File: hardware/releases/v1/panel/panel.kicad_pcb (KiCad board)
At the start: 4 copper layers, 119 x 56 mm, 132 parts, among them J1 12-32V + RS485, J101 Main board, J102 XD_North, J103 XD_East, J104 XD_South, J105 XD_West, J106 PIEZO_NE, J107 PIEZO_NW, J108 PIEZO_SW, J109 PIEZO_SE, J110 DOME_SOCKET, J2 Crown board, J201 Probe T-Header SMD, J3 Probe board, J301 CROWN_RISER, J4 SEN55 PM, J401 Main board, J402 Reflector T-Socket SMD, Q1 AO3400A, Q401 AO3400A, SW1 SERVICE, U1 SCT2400TVBR, U101 SN74LVC2G04DBVR, U102 CD4052BM96, U103 TLV9062IDR, U104 LM393DR2G, U105 TLV9062IDR, U106 MMC5603NJ, U2 LM66100, U3 XIAO ESP32C6, U301 LTR-390UV-01, U302 VEML7700-TT, U4 BMP581, U401 SCD41-D-R2, U402 SGP41-D-R4, U403 SHT40-AD1F-R2, U404 LM393DR2G, U5 LSM6DS3TR-C, U6 AS3935-BQFT, U7 SP3485EN-L/TR, U8 SN74LVC2G04DBVR

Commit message: Add silkscreen connector labels to all PCB variants for improved assembly identification
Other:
- board text added: "+V GND A+ B-"
- board text added: "CROWN"
- board text added: "DOME"
- board text added: "MAIN"
- board text added: "PM"
- board text added: "PROBE"
- board text added: "REFLECTOR"
- board text added: "RST"

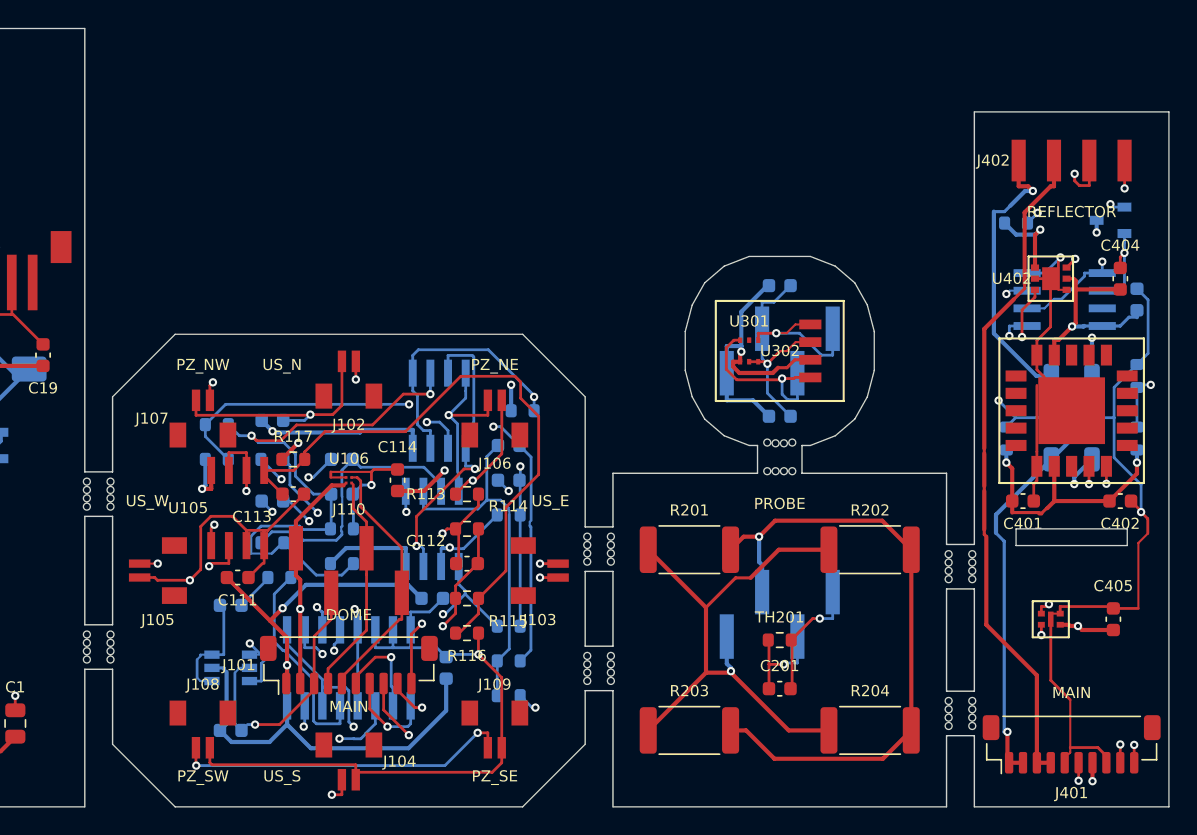
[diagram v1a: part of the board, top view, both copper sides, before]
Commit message: Upgrade dome PCB with enhanced light sensing capabilities: add TSL25911FN visible/NIR sensor and optional GUVB-C31SM UV-B sensor
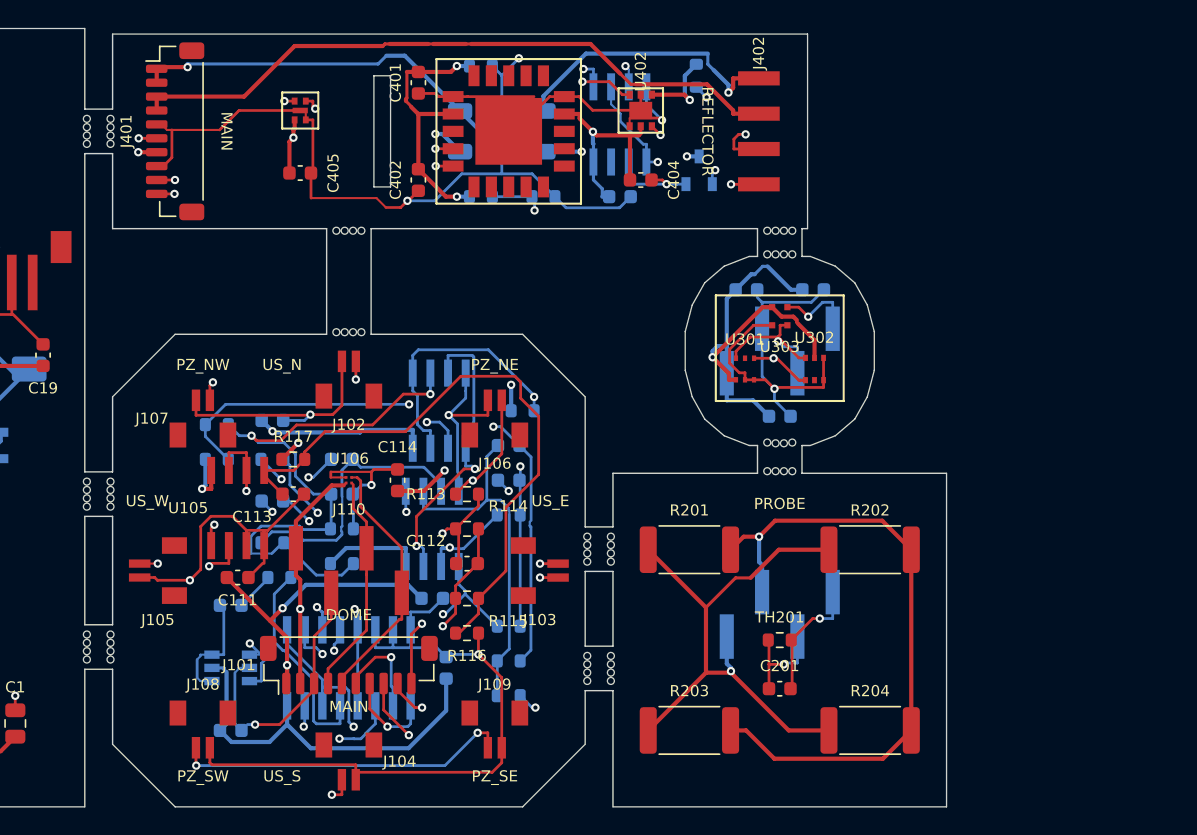
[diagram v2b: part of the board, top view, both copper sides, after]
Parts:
- added C303: 100n 50V, Capacitor_SMD:C_0603_1608Metric, B.Cu at (91.0, -28.1)
- added U303: GUVB-C31SM, gateway_fp:GenUV_GUVB-C31SM, F.Cu at (91.0, -35.3)
- U302: value VEML7700-TT -> TSL25911FN; footprint gateway_fp:Vishay_VEML7700-TT -> gateway_fp:AMS_TSL25911FN
- moved J401 78.1 mm to (47.5, -48.6), turned to -90 degrees
- moved C405 66.7 mm to (56.5, -45.6), turned to 0 degrees
- moved U403 65.2 mm to (56.5, -50.1), turned to -90 degrees
- moved C402 55.5 mm to (65.0, -45.1), turned to -90 degrees
- moved C401 52.9 mm to (65.0, -52.1), turned to -90 degrees
- moved R404 50.3 mm to (69.5, -43.9), turned to 0 degrees
- moved R401 49.9 mm to (68.0, -48.6), turned to -90 degrees
- moved R403 46.3 mm to (69.5, -53.3), turned to 0 degrees
- moved TH401 45.9 mm to (71.0, -48.6), turned to -90 degrees
- moved U401 45.2 mm to (71.5, -48.6), turned to -90 degrees
- moved R405 44.6 mm to (74.0, -43.9), turned to 0 degrees
- moved R402 41.9 mm to (74.0, -48.6), turned to -90 degrees
- moved C403 37.9 mm to (79.5, -43.9), turned to 0 degrees
- moved C404 35.2 mm to (81.0, -45.1), turned to 0 degrees
- moved U404 34.4 mm to (79.5, -49.1), turned to 0 degrees
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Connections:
- U302 pad 1: DOME_I2C_SDA -> DOME_I2C_SCL
- U302 pad 2: DOME_+3V3 -> (no net)
- U302 pad 4: DOME_I2C_SCL -> DOME_GND
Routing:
- net DOME_GND: track 16.5 -> 29.0 mm
- net DOME_+3V3: track 21.9 -> 33.3 mm
- net DOME_I2C_SCL: track 11.1 -> 14.2 mm, vias 1 -> 2
- net DOME_I2C_SDA: track 13.5 -> 11.7 mm
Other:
- board size 119 x 56 mm -> 103 x 56 mm

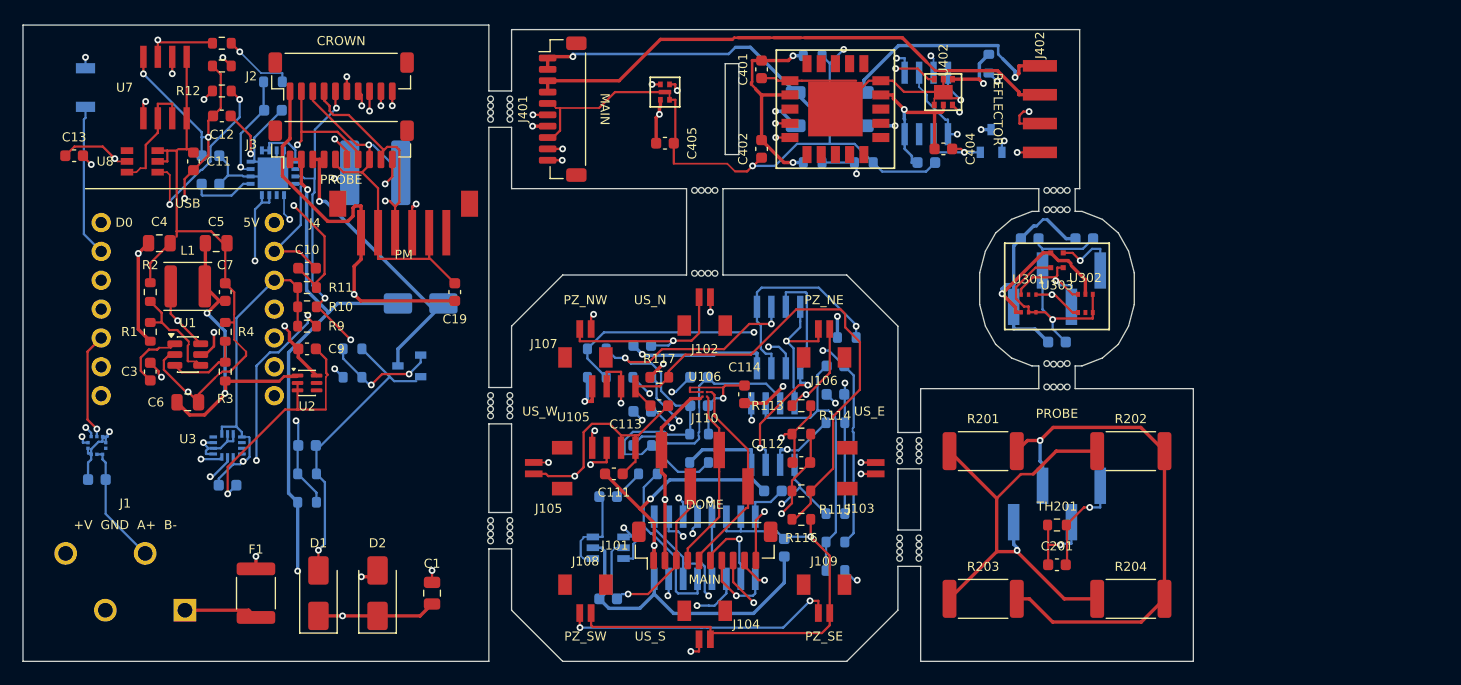
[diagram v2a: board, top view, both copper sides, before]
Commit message: Update enclosure dimensions, add power board, upgrade sensors, and redesign base bay for PMSA003I particulate module
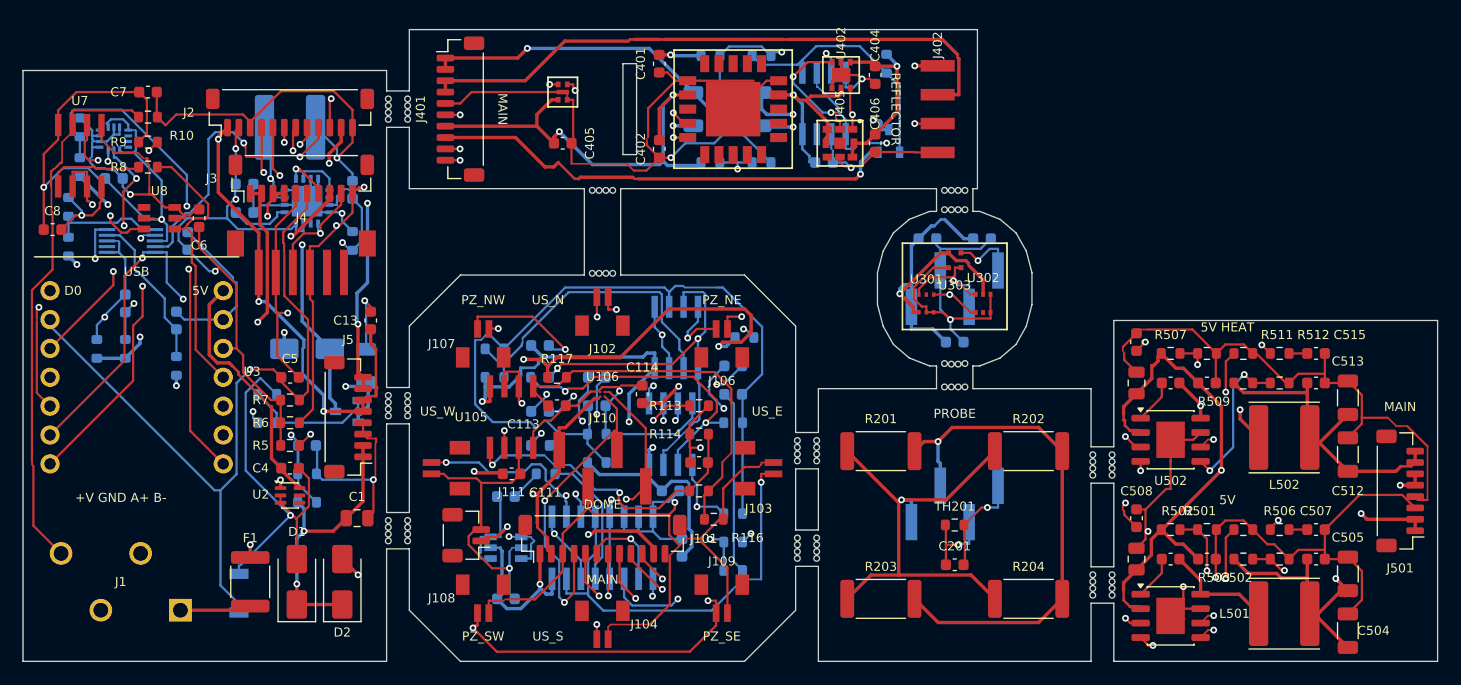
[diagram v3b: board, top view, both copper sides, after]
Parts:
- removed C14, C15, C17: 100n 50V, Capacitor_SMD:C_0603_1608Metric
- removed C16: 1u 50V, Capacitor_SMD:C_0603_1608Metric
- removed C18: 470p C0G 50V, Capacitor_SMD:C_0603_1608Metric
- removed L1: 4.7uH, Inductor_SMD:L_APV_ANR4012
- removed R12: 1k, Resistor_SMD:R_0603_1608Metric
- removed R13, R14: 4k7, Resistor_SMD:R_0603_1608Metric
- removed R15: 10k, Resistor_SMD:R_0603_1608Metric
- removed U1: SCT2400TVBR, Package_TO_SOT_SMD:TSOT-23-6
- added C20: 1u 50V, Capacitor_SMD:C_0603_1608Metric, B.Cu at (9.00, -31.5)
- added C21: 100n 50V, Capacitor_SMD:C_0603_1608Metric, B.Cu at (14.5, -37.0)
- added C406: 100n 50V, Capacitor_SMD:C_0603_1608Metric, F.Cu at (75.0, -45.6)
- added C501: 10u 50V, Capacitor_SMD:C_0805_2012Metric, F.Cu at (98.0, -9.00)
- added C502: 100n 50V, Capacitor_SMD:C_0603_1608Metric, F.Cu at (104.2, -9.00)
- added C503: 100n 50V, Capacitor_SMD:C_0603_1608Metric, F.Cu at (101.0, -9.00)
- added C504: 47u 10V, Capacitor_SMD:C_1206_3216Metric, F.Cu at (116.6, -2.70)
- added C505: 47u 10V, Capacitor_SMD:C_1206_3216Metric, F.Cu at (116.6, -7.70)
- added C506: 100n 50V, Capacitor_SMD:C_0603_1608Metric, F.Cu at (113.8, -9.00)
- added C507: 3n3 50V, Capacitor_SMD:C_0603_1608Metric, F.Cu at (113.8, -11.6)
- added C508: 22p C0G 50V, Capacitor_SMD:C_0603_1608Metric, F.Cu at (98.0, -12.6)
- added C509: 10u 50V, Capacitor_SMD:C_0805_2012Metric, F.Cu at (98.0, -24.5)
- added C510: 100n 50V, Capacitor_SMD:C_0603_1608Metric, F.Cu at (104.2, -24.5)
- added C511: 100n 50V, Capacitor_SMD:C_0603_1608Metric, F.Cu at (101.0, -24.5)
- added C512: 47u 10V, Capacitor_SMD:C_1206_3216Metric, F.Cu at (116.6, -18.2)
- added C513: 47u 10V, Capacitor_SMD:C_1206_3216Metric, F.Cu at (116.6, -23.2)
- added C514: 100n 50V, Capacitor_SMD:C_0603_1608Metric, F.Cu at (113.8, -24.5)
- added C515: 3n3 50V, Capacitor_SMD:C_0603_1608Metric, F.Cu at (113.8, -27.1)
- added C516: 22p C0G 50V, Capacitor_SMD:C_0603_1608Metric, F.Cu at (98.0, -28.1)
- added J111: AUX 5V_HEAT, Connector_JST:JST_SH_BM02B-SRSS-TB_1x02-1MP_P1.00mm_Vertical, F.Cu at (39.0, -11.1)
- added J5: Power board, Connector_JST:JST_SH_BM08B-SRSS-TB_1x08-1MP_P1.00mm_Vertical, F.Cu at (28.6, -21.5)
- added J501: Main board, Connector_JST:JST_SH_BM08B-SRSS-TB_1x08-1MP_P1.00mm_Vertical, F.Cu at (121.2, -15.0)
- added L501: 8.2uH, Inductor_SMD:L_Sunlord_SWPA6045S, F.Cu at (111.0, -4.20)
- added L502: 8.2uH, Inductor_SMD:L_Sunlord_SWPA6045S, F.Cu at (111.0, -19.7)
- added R16: 0R1, Resistor_SMD:R_1206_3216Metric, B.Cu at (30.2, -26.0)
- added R17: 1R, Resistor_SMD:R_0603_1608Metric, B.Cu at (6.50, -27.5)
- added R18: 1k, Resistor_SMD:R_0603_1608Metric, B.Cu at (13.5, -26.0)
- added R19: 1k, Resistor_SMD:R_0603_1608Metric, B.Cu at (9.00, -27.5)
- added R20: 10k, Resistor_SMD:R_0603_1608Metric, B.Cu at (4.00, -36.5)
- added R21: 10k, Resistor_SMD:R_0603_1608Metric, B.Cu at (4.00, -40.0)
- added R24: 10k, Resistor_SMD:R_0603_1608Metric, B.Cu at (5.00, -43.5)
- added R25: 10k, Resistor_SMD:R_0603_1608Metric, B.Cu at (5.00, -47.0)
- added R407: 470k, Resistor_SMD:R_0603_1608Metric, B.Cu at (65.0, -53.3)
- added R501: 51k, Resistor_SMD:R_0603_1608Metric, F.Cu at (101.0, -11.6)
- added R502: 10k, Resistor_SMD:R_0603_1608Metric, F.Cu at (104.2, -11.6)
- added R503: 53k6, Resistor_SMD:R_0603_1608Metric, F.Cu at (107.4, -9.00)
- added R504: 10k2, Resistor_SMD:R_0603_1608Metric, F.Cu at (110.6, -9.00)
- added R505: 200k, Resistor_SMD:R_0603_1608Metric, F.Cu at (107.4, -11.6)
- added R506: 33k2, Resistor_SMD:R_0603_1608Metric, F.Cu at (110.6, -11.6)
- added R507: 51k, Resistor_SMD:R_0603_1608Metric, F.Cu at (101.0, -27.1)
- added R508: 10k, Resistor_SMD:R_0603_1608Metric, F.Cu at (104.2, -27.1)
- added R509: 53k6, Resistor_SMD:R_0603_1608Metric, F.Cu at (107.4, -24.5)
- added R510: 10k2, Resistor_SMD:R_0603_1608Metric, F.Cu at (110.6, -24.5)
- added R511: 200k, Resistor_SMD:R_0603_1608Metric, F.Cu at (107.4, -27.1)
- added R512: 33k2, Resistor_SMD:R_0603_1608Metric, F.Cu at (110.6, -27.1)
- added U405: BMP585, gateway_fp:Bosch_BMP585_LGA-9, F.Cu at (71.9, -45.6)
- added U501: SCT2430STER, Package_SO:SOIC-8-1EP_3.9x4.9mm_P1.27mm_EP2.514x3.2mm, F.Cu at (101.0, -4.00)
- added U502: SCT2430STER, Package_SO:SOIC-8-1EP_3.9x4.9mm_P1.27mm_EP2.514x3.2mm, F.Cu at (101.0, -19.5)
- C10: value 100n 50V -> 1u 50V; moved to B.Cu
- C11, C3, R11, R2: moved to B.Cu
- C12: value 100n 50V -> 470p C0G 50V; moved to B.Cu
- C13: value 100n 50V -> 10u 10V
- C19: value 10u 10V -> 1u 50V; moved to B.Cu
- C303: value 100n 50V -> 1u 50V
- C4: value 10u 50V -> 10u 10V; footprint Capacitor_SMD:C_0805_2012Metric -> Capacitor_SMD:C_0603_1608Metric
- C5, C6: value 22u 25V -> 100n 50V; footprint Capacitor_SMD:C_0805_2012Metric -> Capacitor_SMD:C_0603_1608Metric
- C8: moved to F.Cu
- C9: value 10u 10V -> 100n 50V; moved to B.Cu
- J101, J2: footprint Connector_JST:JST_SH_BM10B-SRSS-TB_1x10-1MP_P1.00mm_Vertical -> Connector_JST:JST_SH_BM12B-SRSS-TB_1x12-1MP_P1.00mm_Vertical
- J4: value SEN55 PM -> PMSA003I PM
- R1: value 51k -> 100k; moved to B.Cu
- R201, R202, R203, R204: value 100R -> 27R
- R3: value 51k -> 330R; moved to B.Cu
- R4: value 10k -> 100k; moved to B.Cu
- R401, R402: value 470R -> 120R
- R5: value 100k -> 4k7; moved to F.Cu
- R6: value 10k -> 4k7; moved to F.Cu
- R7: value 330R -> 10k; moved to F.Cu
- R8: value 100k -> 1k; moved to F.Cu
- U4: value BMP581 -> ADS1115IDGSR; footprint gateway_fp:Bosch_BMP581_LGA-10 -> gateway_fp:TI_ADS1115_VSSOP-10
- moved SW1 46.5 mm to (19.0, -6.00)
- moved C13 29.9 mm to (30.6, -30.0), turned to 90 degrees
- moved C8 29.4 mm to (2.60, -38.0)
- moved U5 28.8 mm to (8.00, -46.0)
- moved C19 24.6 mm to (13.5, -30.0)
- moved R8 24.1 mm to (11.0, -43.5)
- moved C4 22.9 mm to (23.5, -17.0)
- moved C9 22.7 mm to (8.00, -42.5)
- moved R10 21.8 mm to (11.0, -47.9)
- moved R9 21.4 mm to (11.0, -45.7)
- moved R2 21.1 mm to (25.0, -16.5), turned to 0 degrees
- moved R1 20.4 mm to (25.0, -14.0), turned to 0 degrees
- moved C7 18.9 mm to (11.0, -50.1), turned to 0 degrees
- moved U4 18.2 mm to (9.50, -37.0), turned to 90 degrees
- moved C6 16.2 mm to (15.5, -39.0), turned to 90 degrees
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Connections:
- net PROBE_VIN_PROT renamed PROBE_+5V_HEAT
- net REFLECTOR_VIN_PROT renamed REFLECTOR_+5V_HEAT
- C10 pad 1: NTC_SENSE -> AS_ACG
- C12 pad 1: +3V3 -> AS_INP
- C13 pad 1: +3V3 -> +5V
- C19 pad 1: +5V -> MON_REFL
- C3 pad 1: BUCK5_BST -> VIN_ADC
- C3 pad 2: BUCK5_SW -> GND
- C4 pad 1: VIN_PROT -> +5V_XIAO
- C5 pad 1: +5V -> NTC_SENSE
- C6 pad 1: +5V -> +3V3
- C7 pad 1: +5V -> +3V3
- C8 pad 1: VIN_ADC -> +3V3
- C9 pad 1: +5V_XIAO -> +3V3
- D3 pad 1: VIN_PROT -> +5V_HEAT
- J3 pad 1: VIN_PROT -> +5V_HEAT
- J3 pad 2: VIN_PROT -> +5V_HEAT
- J3 pad 8: GND -> CO2_HEAT_RTN
- J4 pad 5: GND -> (no net)
- J401 pad 8: PROBE_GND -> PROBE_CO2_HEAT_RTN
- Q1 pad 2: GND -> HEAT_SENSE
- Q401 pad 2: PROBE_GND -> PROBE_CO2_HEAT_RTN
- R1 pad 2: BUCK5_EN -> VIN_ADC
- R10 pad 1: +3V3 -> RS485_B
- R10 pad 2: I2C_SCL -> GND
- R11 pad 1: +3V3 -> AS_INP
- R11 pad 2: NTC_SENSE -> GND
- R2 pad 1: BUCK5_EN -> VIN_ADC
- R3 pad 1: +5V -> HEAT_PWM
- R3 pad 2: BUCK5_FB -> HEAT_GATE
- R4 pad 1: BUCK5_FB -> HEAT_GATE
- R5 pad 1: VIN_PROT -> +3V3
- R5 pad 2: VIN_ADC -> I2C_SDA
- R6 pad 1: VIN_ADC -> +3V3
- R6 pad 2: GND -> I2C_SCL
- R7 pad 1: HEAT_PWM -> +3V3
- R7 pad 2: HEAT_GATE -> NTC_SENSE
- R8 pad 1: HEAT_GATE -> RS485_RO
- R8 pad 2: GND -> RS485_IO
- R9 pad 2: I2C_SDA -> RS485_A
- U4 pad 1: +3V3 -> GND
- U4 pad 10: +3V3 -> I2C_SCL
- U4 pad 2: I2C_SCL -> (no net)
- U4 pad 4: I2C_SDA -> MON_REFL
- U4 pad 5: +3V3 -> MON_PROBE
- U4 pad 6: +3V3 -> MON_5V
- U4 pad 7: (no net) -> MON_5V_LOGIC
- U4 pad 8: GND -> +3V3
- U4 pad 9: GND -> I2C_SDA
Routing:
- net POWER_GND: track 0.00 -> 102.1 mm, vias 0 -> 3
- net VIN_PROT: track 103.2 -> 24.7 mm, vias 5 -> 2
- net +5V_HEAT: track 0.00 -> 71.9 mm, vias 0 -> 6
- net POWER_VIN_PROT: track 0.00 -> 63.4 mm, vias 0 -> 2
- net PROBE_CO2_HEAT_RTN: track 0.00 -> 41.6 mm, vias 0 -> 1
- net POWER_+5V: track 0.00 -> 34.7 mm, vias 0 -> 2
- net I2C_SDA: track 82.6 -> 114.7 mm
- net POWER_LOGIC_COMP: track 0.00 -> 30.1 mm, vias 0 -> 3
- net CO2_HEAT_RTN: track 0.00 -> 27.4 mm, vias 0 -> 2
- net POWER_+5V_HEAT: track 0.00 -> 27.1 mm
- net MON_5V_LOGIC: track 0.00 -> 26.3 mm, vias 0 -> 2
- net POWER_HEAT_COMP: track 0.00 -> 25.1 mm, vias 0 -> 3
- net HEAT_SENSE: track 0.00 -> 23.7 mm, vias 0 -> 2
- net CROWN_PIEZO_IN: track 85.6 -> 105.8 mm, vias 4 -> 5
- net POWER_HEAT_RT: track 0.00 -> 17.6 mm, vias 0 -> 2
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- added copper zone on In1.Cu, net POWER_GND
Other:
- board size 103 x 56 mm -> 124.5 x 55.6 mm
- board text added: "5V"
- board text added: "5V HEAT"
